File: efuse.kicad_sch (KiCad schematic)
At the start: 6 parts, among them SW1 PTS810_SJM_250_SMTR_LFS, U2 TPS259630

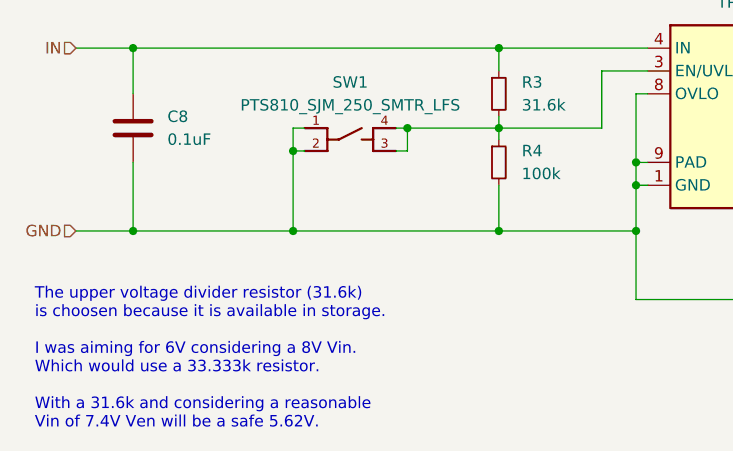
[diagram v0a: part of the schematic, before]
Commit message: sch: change undervoltage resistor value
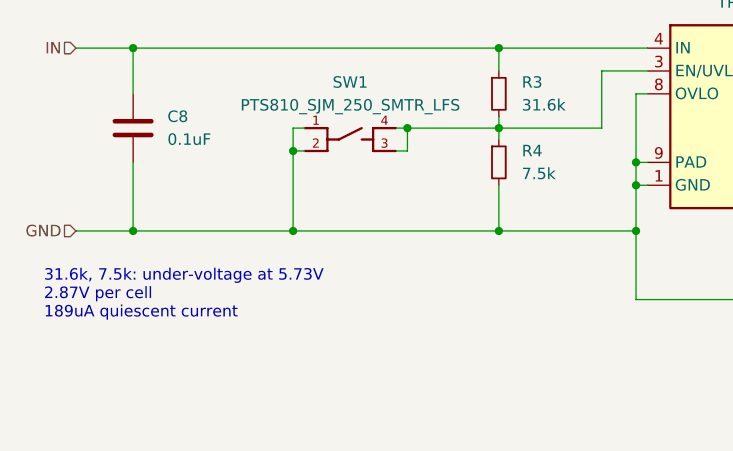
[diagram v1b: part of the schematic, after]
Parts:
- R4: value 100k -> 7.5k
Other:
- note added: "31.6k, 7.5k: under-voltage at 5.73V 2.87V per cell 189uA quiescent current"
- note removed: "The upper voltage divider resistor (31.6k) is choosen because it is available in storage. I was aiming for 6V considering a 8V Vin. Which would use a 33.333k resistor. With a 31.6k and considering a reasonable Vin of 7.4V Ven will be a safe 5.62V."
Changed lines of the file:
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@@
 		)
 	)
-	(text "The upper voltage divider resistor (31.6k)\nis choosen because it is available in storage.\n\nI was aiming for 6V considering a 8V Vin.\nWhich would use a 33.333k resistor.\n\nWith a 31.6k and considering a reasonable\nVin of 7.4V Ven will be a safe 5.62V."
+	(text "31.6k, 7.5k: under-voltage at 5.73V\n2.87V per cell\n189uA quiescent current"
 		(exclude_from_sim no)
-		(at 20.828 59.944 0)
+		(at 21.844 52.832 0)
 		(effects
 			(font
@@
 			)
 		)
-		(property "Value" "100k"
+		(property "Value" "7.5k"
 			(at 74.93 39.3699 0)
 			(effects

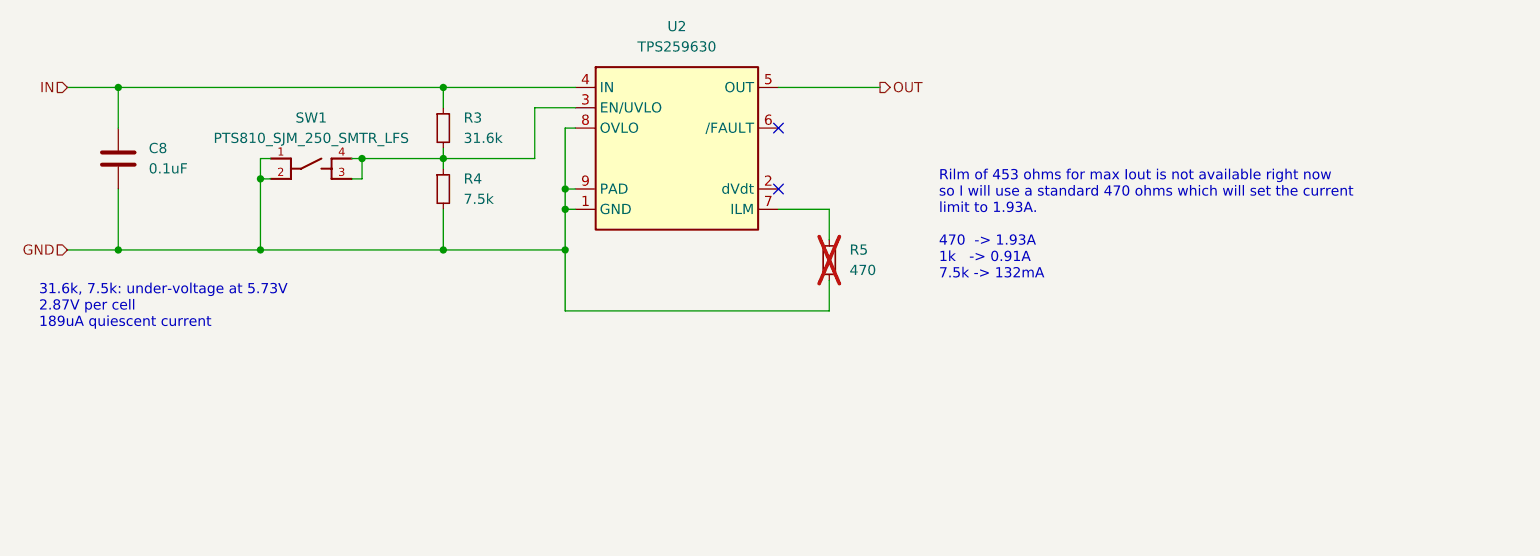
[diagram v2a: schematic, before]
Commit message: Add clarity to the choice resistors
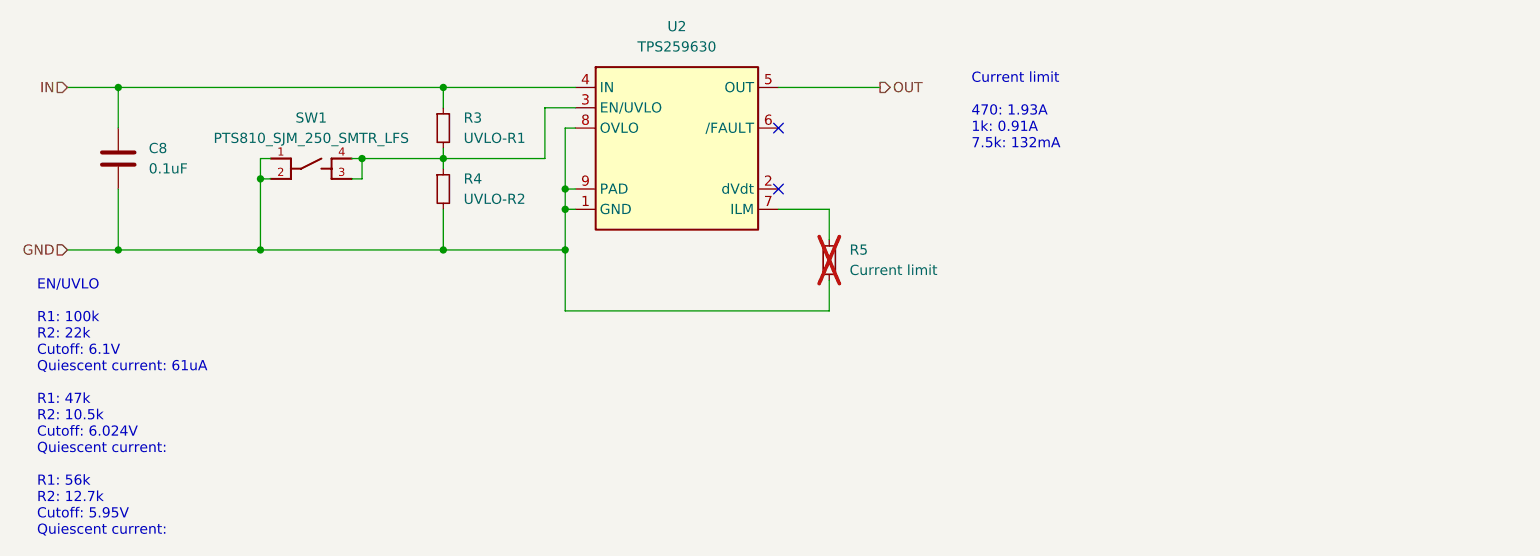
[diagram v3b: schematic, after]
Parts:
- R3: value 31.6k -> UVLO-R1
- R4: value 7.5k -> UVLO-R2
- R5: value 470 -> Current limit
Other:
- note added: "Current limit 470: 1.93A 1k: 0.91A 7.5k: 132mA"
- note added: "EN/UVLO R1: 100k R2: 22k Cutoff: 6.1V Quiescent current: 61uA R1: 47k R2: 10.5k Cutoff: 6.024V Quiescent current: R1: 56k R2: 12.7k Cutoff: 5.95V Quiescent current:"
- note removed: "31.6k, 7.5k: under-voltage at 5.73V 2.87V per cell 189uA quiescent current"
- note removed: "Rilm of 453 ohms for max Iout is not available right now so I will use a standard 470 ohms which will set the current limit to 1.93A. 470 -> 1.93A 1k -> 0.91A 7.5k -> 132mA"
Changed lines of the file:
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@@
 	(wire
 		(pts
-			(xy 72.39 34.29) (xy 83.82 34.29)
+			(xy 72.39 34.29) (xy 85.09 34.29)
 		)
 		(stroke
@@
 	(wire
 		(pts
-			(xy 83.82 34.29) (xy 83.82 27.94)
+			(xy 85.09 34.29) (xy 85.09 27.94)
 		)
 		(stroke
@@
 	(wire
 		(pts
-			(xy 83.82 27.94) (xy 88.9 27.94)
+			(xy 85.09 27.94) (xy 88.9 27.94)
 		)
 		(stroke
@@
 		)
 	)
-	(text "Rilm of 453 ohms for max Iout is not available right now\nso I will use a standard 470 ohms which will set the current\nlimit to 1.93A.\n\n470  -> 1.93A\n1k   -> 0.91A\n7.5k -> 132mA"
+	(text "Current limit\n\n470: 1.93A\n1k: 0.91A\n7.5k: 132mA"
 		(exclude_from_sim no)
-		(at 134.366 42.672 0)
+		(at 138.43 28.448 0)
 		(effects
 			(font
@@
 		)
 	)
-	(text "31.6k, 7.5k: under-voltage at 5.73V\n2.87V per cell\n189uA quiescent current"
+	(text "EN/UVLO\n\nR1: 100k\nR2: 22k\nCutoff: 6.1V\nQuiescent current: 61uA\n\nR1: 47k\nR2: 10.5k\nCutoff: 6.024V\nQuiescent current: \n\nR1: 56k\nR2: 12.7k\nCutoff: 5.95V\nQuiescent current: "
 		(exclude_from_sim no)
-		(at 21.844 52.832 0)
+		(at 21.59 65.532 0)
 		(effects
 			(font
@@
 			)
 		)
-		(property "Value" "7.5k"
+		(property "Value" "UVLO-R2"
 			(at 74.93 39.3699 0)
 			(effects
@@
 			)
 		)
-		(property "Value" "31.6k"
+		(property "Value" "UVLO-R1"
 			(at 74.93 31.7499 0)
 			(effects
@@
 			)
 		)
-		(property "Value" "470"
+		(property "Value" "Current limit"
 			(at 123.19 48.2599 0)
 			(effects
